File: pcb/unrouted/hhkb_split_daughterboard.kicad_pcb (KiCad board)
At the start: 2 copper layers, 21 x 32 mm, 11 parts

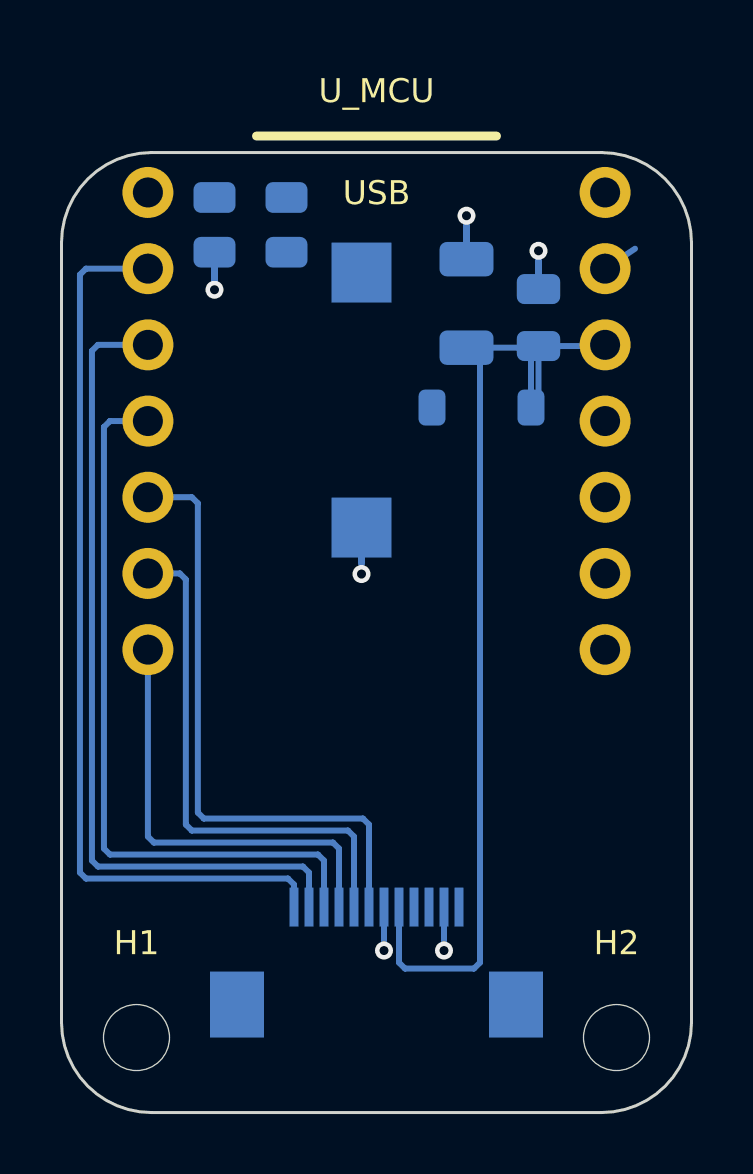
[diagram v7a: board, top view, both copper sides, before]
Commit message: 子基板の右列を、左列の鏡像として自分で引いた
利用者の指示「D1〜D6 を完璧に真似る形で、左右対称に」。右列は
Freerouting 任せだったので、左列と同じ規則で引くようにした。

XIAO は x=150.0 を挟んで左右対称なので、**鏡像は同じ y のパッドどうし**
（D1↔GND / D2↔3V3 / D3↔D10 / D4↔D9 / D5↔D8 / D6↔D7）。FFC は
n ↔ 13-n で写る。`_prewire_rows` に `side`（-1 左 / +1 右）を入れ、
左向きの直書き（min・-DB_W/2）を符号 1 つに畳んだ。

指摘を 3 つ受けて直した:
  - D7 が垂直に伸びていない … D6 の鏡像は D7。GND を外したことと
    垂直の有無は無関係だった
  - D4 の鏡像は D9 … 内側の順序を左列の鏡像 (D7,D8,D9) に揃えた
  - V3V3 が 2 経路で FFC に繋がる … `_prewire_power` の旧経路を削除。
    3V3 パッド ↔ FFC 2 番はレーンが引くので二重だった

**GND はレーンに載せず地板で受ける**（利用者の判断）。そのぶん外側は
2 本になるが、**位置は 3 本ぶんの幅に散らして真ん中を空ける**——
利用者の指示「D10 と離す意図で、鏡像の 3 本ラインの左端と右端と同様に」。
電源とデータ線の並走結合を、空いている枠を使って 0 コストで下げる。

⚠️ **この組み替えでケーブルの GND が 2 本から 1 本になった。**
SCK から最寄りの GND までが 0.5mm → 2.0mm に伸びている。効くのは
遷移が速い SCK 1 本で、どれだけ悪化するかは実測していない。
逃げ道は決めてある（D9=SPARE2 を両基板で GND へジャンパ）。

検査は「GND が 2 本」を数えるのをやめ、**距離そのもの**を見るように
書き換えた（`test_how_far_the_return_path_is`）。本数は手段で、目的は
戻り経路の短さ。故意に壊して距離 7 で落ちることを確認した。
`test_the_rules_actually_bite` の変異 1 件が**元と同じ値を代入する
空振り**になっていたのも、その検査自身が捕まえたので直した。

子基板 DRC: 違反 0 / 未配線 0。保留していた V3V3-GND の 0.100mm も
旧経路の削除で消えた。主基板の SPARE/SPARE2 が片側 1 ピンなので
test_circuit が 2 件赤。左右の基板はこれから直す。

Co-Authored-By: Claude Opus 5 (1M context) <noreply@anthropic.com>
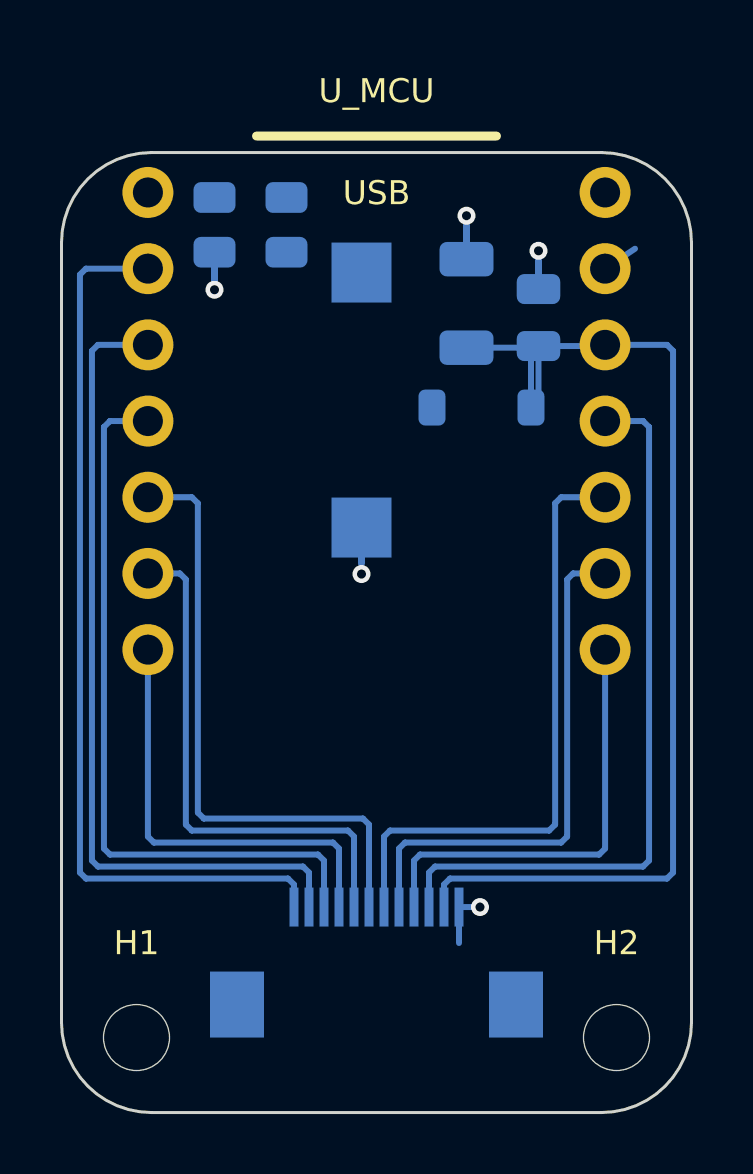
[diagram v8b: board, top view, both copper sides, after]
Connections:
- J_MAIN pad 1: CS -> GND
- J_MAIN pad 2: GND -> V3V3
- J_MAIN pad 3: SPI_SCK -> SPI_MOSI
- J_MAIN pad 4: SPI_MOSI -> CS
- J_MAIN pad 5: V3V3 -> SPI_SCK
- J_MAIN pad 6: GND -> SPARE2
- U_MCU pad D9: (no net) -> SPARE2
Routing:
- net SPI_MOSI: track 0.00 -> 24.6 mm
- net SPARE2: track 0.00 -> 20.7 mm
- net SPI_SCK: track 0.00 -> 17.6 mm
- net CS: track 0.00 -> 14.7 mm
- net GND: track 16.8 -> 13.4 mm, vias 6 -> 5
- net V3V3: track 34.2 -> 37.0 mm
